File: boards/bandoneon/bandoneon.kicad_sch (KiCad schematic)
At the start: 11 parts, among them J1 AudioJack3, J2 AudioJack3, J3 JST XH-3A, J4 JST XH-3A, J6 2D JOYSTICK, J6 JST XH-3A, J8 JST XH-3A, U10 Feather M4 Express

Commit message: Manual routing
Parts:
- renumbered J6 to J1, J6 to J2, J8 to J3, J1 to J4, J2 to J5, J3 to J6, J4 to J7, RV4 to RV1, RV5 to RV2, U10 to U1
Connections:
- net 3V3 is gone; now on net +3.3V: J6.3 (Pin_3), J7.3 (Pin_3)
- net G1/MISO: now also U1.22 ((10)PA20); no longer U1.18 ((22)PA13)
- net G10/MISO: now also U1.11 (PA17(25)); no longer U1.21 ((9)PA19)
- net G2/MISO: now also U1.21 ((9)PA19); no longer U1.16 (PA14(4))
- net G3/MISO: now also U1.19 ((5)PA16); no longer U1.11 (PA17(25))
- net G4/MISO: now also U1.20 ((6)PA18); no longer U1.10 (PA06(19/A5))
- net G5/MISO: now also U1.18 ((22)PA13); no longer U1.17 ((21)PA12)
- net G6/MISO: now also U1.16 (PA14(4)); no longer U1.19 ((5)PA16)
- net G7/MISO: now also U1.10 (PA06(19/A5)); no longer U1.20 ((6)PA18)
- net G9/MISO: now also U1.17 ((21)PA12); no longer U1.22 ((10)PA20)
- net JOY_BT: now also U1.15 (PB16(1)); no longer U1.14 (PB17(0))
- net SUS_PED: now also U1.14 (PB17(0)); no longer U1.15 (PB16(1))

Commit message: Wiring fixed
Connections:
- net JOY_X: now also U1.8 (PB09(17/A3)); no longer U1.5 (PA02(14/A0))
- net JOY_Y: now also U1.9 (PA04(18/A4)); no longer U1.6 (PA05(15/A1))
- net P1: now also U1.6 (PA05(15/A1)); no longer U1.8 (PB09(17/A3))
- net P2: now also U1.5 (PA02(14/A0)); no longer U1.9 (PA04(18/A4))
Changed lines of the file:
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@@
+    (stroke (width 0) (type default))
+  )
+  (wire (pts (xy 170.18 91.44) (xy 171.45 91.44))
     (stroke (width 0) (type default))
   )
@@
     (stroke (width 0) (type default))
   )
+  (wire (pts (xy 170.18 88.9) (xy 171.45 88.9))
+    (stroke (width 0) (type default))
+  )
   (wire (pts (xy 222.25 64.77) (xy 224.79 64.77))
     (stroke (width 0) (type default))
@@
     (effects (font (size 1.27 1.27)) (justify right bottom))
   )
-  (label "JOY_X" (at 170.18 81.28 180) (fields_autoplaced)
+  (label "JOY_X" (at 170.18 88.9 180) (fields_autoplaced)
     (effects (font (size 1.27 1.27)) (justify right bottom))
   )
@@
     (effects (font (size 1.27 1.27)) (justify left bottom))
   )
-  (label "JOY_Y" (at 170.18 83.82 180) (fields_autoplaced)
+  (label "JOY_Y" (at 170.18 91.44 180) (fields_autoplaced)
     (effects (font (size 1.27 1.27)) (justify right bottom))
   )
@@
     (effects (font (size 1.27 1.27)) (justify left bottom))
   )
-  (label "P2" (at 171.45 91.44 180) (fields_autoplaced)
+  (label "P2" (at 170.18 81.28 180) (fields_autoplaced)
     (effects (font (size 1.27 1.27)) (justify right bottom))
   )
@@
     (effects (font (size 1.27 1.27)) (justify left bottom))
   )
-  (label "P1" (at 171.45 88.9 180) (fields_autoplaced)
-    (effects (font (size 1.27 1.27)) (justify right bottom))
-  )
+  (label "P1" (at 170.18 83.82 180) (fields_autoplaced)
+    (effects (font (size 1.27 1.27)) (justify right bottom))
+  )

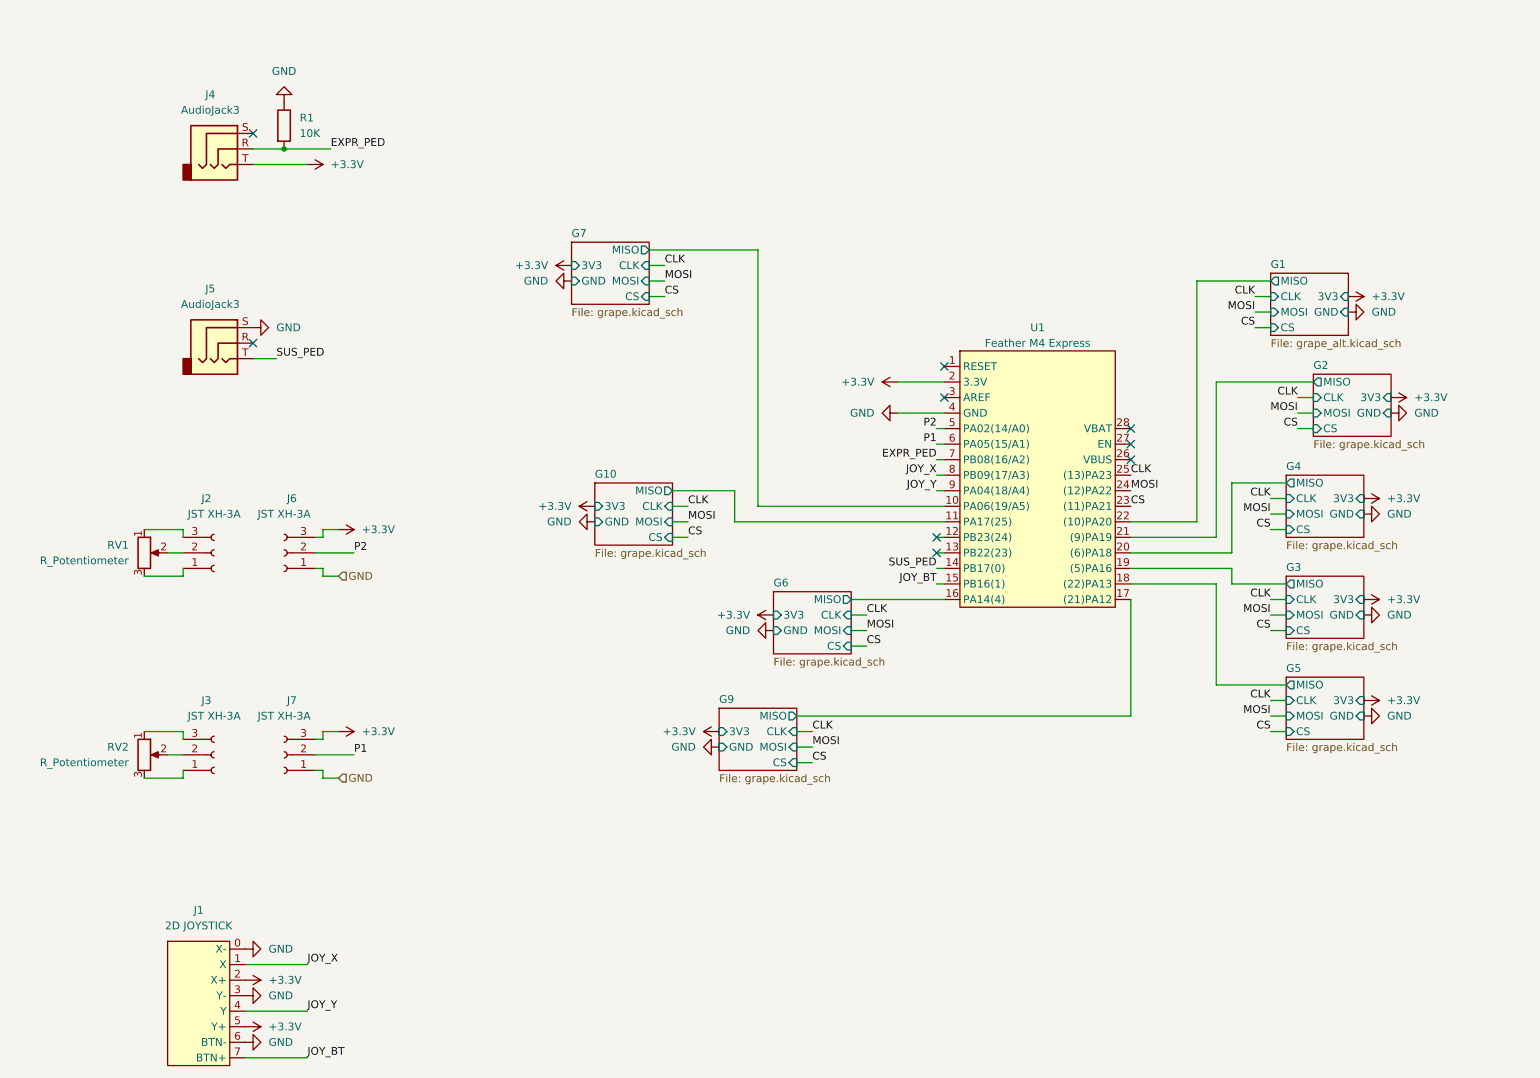
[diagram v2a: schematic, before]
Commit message: Add esd protection
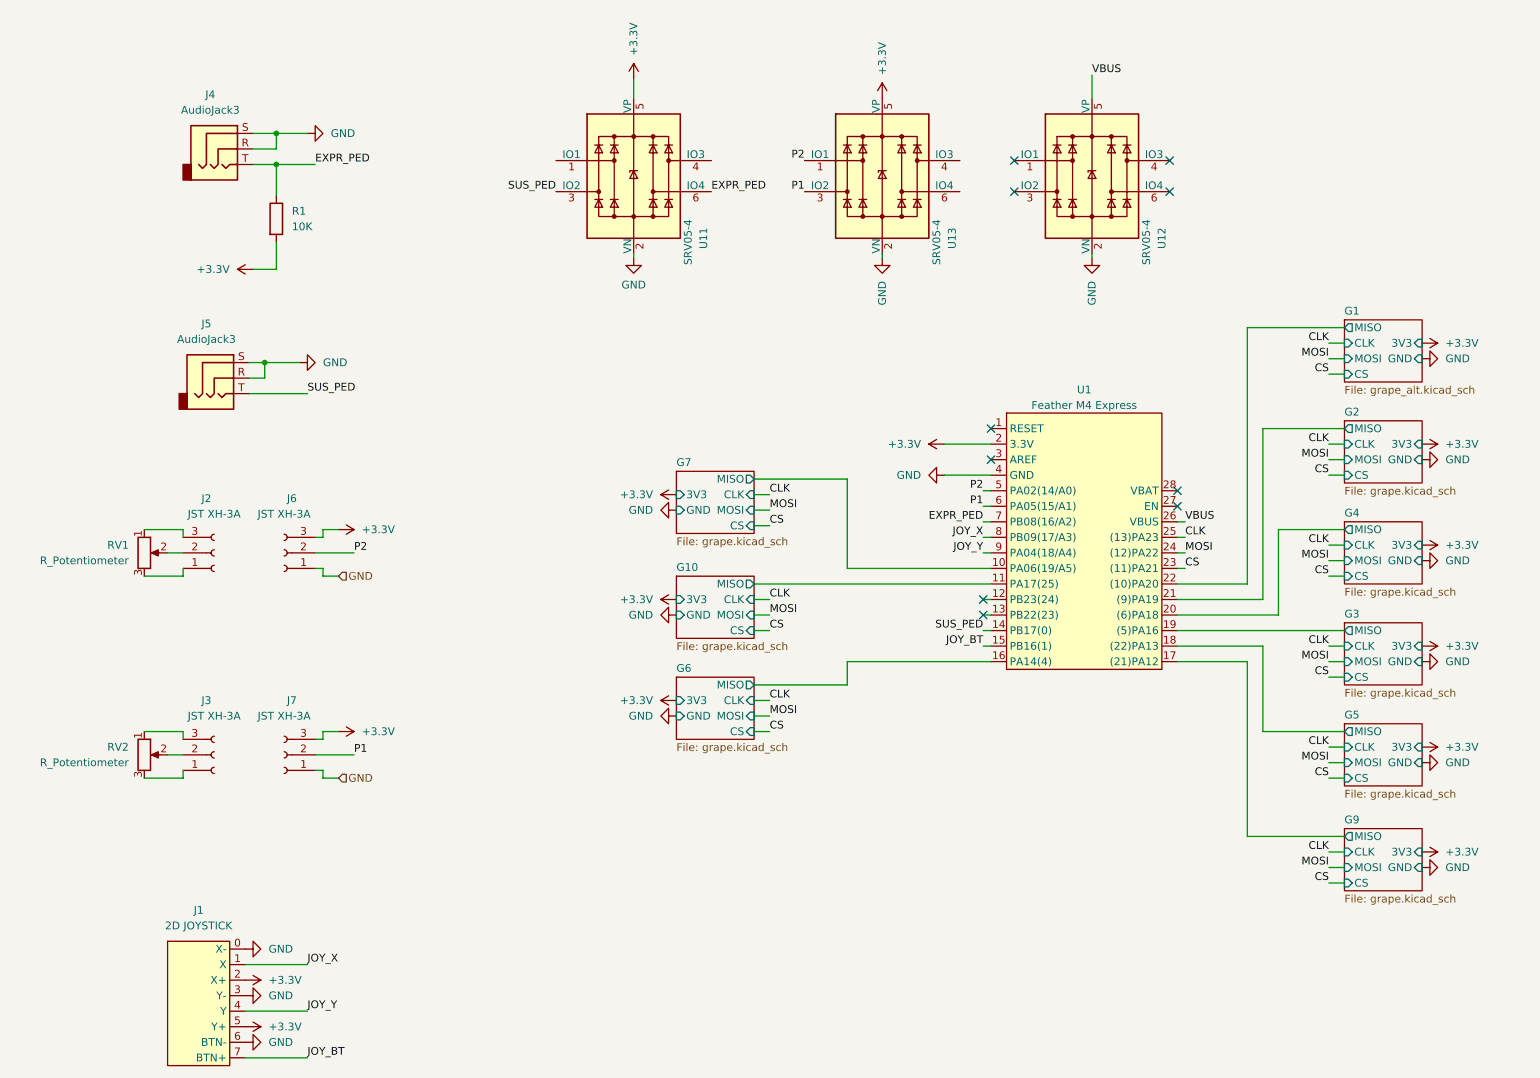
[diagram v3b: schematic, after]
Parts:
- added U11, U12, U13: SRV05-4, Package_TO_SOT_SMD:SOT-23-6, symbol Power_Protection:SRV05-4
- R1: LCSC (none) -> C25804
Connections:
- net +3.3V: now also R1.2, U11.5 (VP), U13.5 (VP); no longer J4.T
- net EXPR_PED: now also J4.T, R1.1, U11.6 (IO4); no longer J4.R, R1.2
- net GND: now also J4.R, J4.S, J5.R, U11.2 (VN), U12.2 (VN), U13.2 (VN); no longer R1.1
- net P1: now also U13.3 (IO2)
- net P2: now also U13.1 (IO1)
- net SUS_PED: now also U11.3 (IO2)
- net VBUS: now reaches U1.26 (VBUS)
- net VBUS: now also U12.5 (VP)
- no-connect marks 9 -> 10
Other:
- moved on the sheet: J5, R1, U1

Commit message: Gerber and bom export
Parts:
- J1, J2, J3, J4, J5, J6, J7, RV1, RV2, U1: now left out of the parts list
- R1: LCSC C25804 -> (none); LCSC Part (none) -> C25804
- U11, U12, U13: LCSC C2836319 -> (none); LCSC Part (none) -> C2836319
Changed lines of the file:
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@@
   )
   (symbol (lib_id "Connector:Conn_01x03_Socket") (at 63.5 101.6 180) (unit 1)
-    (in_bom yes) (on_board yes) (dnp no)
+    (in_bom no) (on_board yes) (dnp no)
     (property "Reference" "J6" (at 64.77 92.71 0)
       (effects (font (size 1.27 1.27)))
@@
   )
   (symbol (lib_id "Connector_Audio:AudioJack3") (at 52.705 73.025 0) (unit 1)
-    (in_bom yes) (on_board yes) (dnp no) (fields_autoplaced)
+    (in_bom no) (on_board yes) (dnp no) (fields_autoplaced)
     (property "Reference" "J5" (at 50.8 64.135 0)
       (effects (font (size 1.27 1.27)))
@@
   )
   (symbol (lib_id "Connector:Conn_01x03_Socket") (at 52.07 134.62 0) (mirror x) (unit 1)
-    (in_bom yes) (on_board no) (dnp no)
+    (in_bom no) (on_board no) (dnp no)
     (property "Reference" "J3" (at 50.8 125.73 0)
       (effects (font (size 1.27 1.27)))
@@
       (effects (font (size 1.27 1.27)) hide)
     )
-    (property "Datasheet" "https://www.lcsc.com/datasheet/lcsc_datasheet_2202221730_MSKSEMI-SRV05-4_C2836319.pdf" (at 120.65 40.005 0)
+    (property "Datasheet" "http://www.onsemi.com/pub/Collateral/SRV05-4-D.PDF" (at 120.65 40.005 0)
       (effects (font (size 1.27 1.27)) hide)
     )
@@
       (effects (font (size 1.27 1.27)) hide)
     )
-    (property "LCSC" "C2836319" (at 120.65 40.005 90)
+    (property "LCSC Part" "C2836319" (at 120.65 40.005 90)
       (effects (font (size 1.27 1.27)) hide)
     )
@@
   )
   (symbol (lib_id "Device:R_Potentiometer") (at 40.64 101.6 0) (unit 1)
-    (in_bom yes) (on_board no) (dnp no) (fields_autoplaced)
+    (in_bom no) (on_board no) (dnp no) (fields_autoplaced)
     (property "Reference" "RV1" (at 38.1 100.33 0)
       (effects (font (size 1.27 1.27)) (justify right))
@@
   )
   (symbol (lib_id "Connector:Conn_01x03_Socket") (at 52.07 101.6 0) (mirror x) (unit 1)
-    (in_bom yes) (on_board no) (dnp no)
+    (in_bom no) (on_board no) (dnp no)
     (property "Reference" "J2" (at 50.8 92.71 0)
       (effects (font (size 1.27 1.27)))
@@
       (effects (font (size 1.27 1.27)) hide)
     )
-    (property "Datasheet" "https://www.lcsc.com/datasheet/lcsc_datasheet_2202221730_MSKSEMI-SRV05-4_C2836319.pdf" (at 195.58 40.005 0)
+    (property "Datasheet" "http://www.onsemi.com/pub/Collateral/SRV05-4-D.PDF" (at 195.58 40.005 0)
       (effects (font (size 1.27 1.27)) hide)
     )
@@
       (effects (font (size 1.27 1.27)) hide)
     )
-    (property "LCSC" "C2836319" (at 195.58 40.005 90)
+    (property "LCSC Part" "C2836319" (at 195.58 40.005 90)
       (effects (font (size 1.27 1.27)) hide)
     )
@@
   )
   (symbol (lib_id "Device:R_Potentiometer") (at 40.64 134.62 0) (unit 1)
-    (in_bom yes) (on_board no) (dnp no) (fields_autoplaced)
+    (in_bom no) (on_board no) (dnp no) (fields_autoplaced)
     (property "Reference" "RV2" (at 38.1 133.35 0)
       (effects (font (size 1.27 1.27)) (justify right))
@@
   )
   (symbol (lib_id "Connector:Conn_01x03_Socket") (at 63.5 134.62 180) (unit 1)
-    (in_bom yes) (on_board yes) (dnp no)
+    (in_bom no) (on_board yes) (dnp no)
     (property "Reference" "J7" (at 64.77 125.73 0)
       (effects (font (size 1.27 1.27)))
@@
       (effects (font (size 1.27 1.27)) hide)
     )
-    (property "Datasheet" "https://www.lcsc.com/datasheet/lcsc_datasheet_2202221730_MSKSEMI-SRV05-4_C2836319.pdf" (at 161.29 40.005 0)
+    (property "Datasheet" "http://www.onsemi.com/pub/Collateral/SRV05-4-D.PDF" (at 161.29 40.005 0)
       (effects (font (size 1.27 1.27)) hide)
     )
@@
       (effects (font (size 1.27 1.27)) hide)
     )
-    (property "LCSC" "C2836319" (at 161.29 40.005 90)
+    (property "LCSC Part" "C2836319" (at 161.29 40.005 90)
       (effects (font (size 1.27 1.27)) hide)
     )
@@
   )
   (symbol (lib_id "Connector_Audio:AudioJack3") (at 53.34 35.56 0) (unit 1)
-    (in_bom yes) (on_board yes) (dnp no) (fields_autoplaced)
+    (in_bom no) (on_board yes) (dnp no) (fields_autoplaced)
     (property "Reference" "J4" (at 51.435 26.67 0)
       (effects (font (size 1.27 1.27)))
@@
   )
   (symbol (lib_id "Library:2-Axis_Joystick") (at 49.53 172.72 0) (unit 1)
-    (in_bom yes) (on_board yes) (dnp no)
+    (in_bom no) (on_board yes) (dnp no)
     (property "Reference" "J1" (at 49.53 160.02 0)
       (effects (font (size 1.27 1.27)))
@@
   )
   (symbol (lib_id "Library:Adafruit_Feather_M4_Express") (at 194.31 90.17 0) (unit 1)
-    (in_bom yes) (on_board yes) (dnp no)
+    (in_bom no) (on_board yes) (dnp no)
     (property "Reference" "U1" (at 194.31 74.93 0)
       (effects (font (size 1.27 1.27)))
@@
       (effects (font (size 1.27 1.27)) hide)
     )
-    (property "LCSC" "C25804" (at 62.23 46.99 0)
-      (effects (font (size 1.27 1.27)) hide)
-    )
+    (property "LCSC Part" "C25804" (at 62.23 46.99 0)
+      (effects (font (size 1.27 1.27)) hide)
+    )

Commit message: PCB order
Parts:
- R1: footprint Resistor_SMD:R_0201_0603Metric -> Resistor_SMD:R_0603_1608Metric
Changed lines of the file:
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@@
       (effects (font (size 1.27 1.27)) (justify left))
     )
-    (property "Footprint" "Resistor_SMD:R_0201_0603Metric" (at 60.452 46.99 90)
+    (property "Footprint" "Resistor_SMD:R_0603_1608Metric" (at 60.452 46.99 90)
       (effects (font (size 1.27 1.27)) hide)
     )
